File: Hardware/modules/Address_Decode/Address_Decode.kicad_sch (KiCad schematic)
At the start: 28 parts, among them J1 Bus_PCI_6502, J2 Clock_Sel, SW1 Manual_Clock, U1 74HC14, U2 74HC00, U3 74LS20, U4 DS1501YZ, U5 74LS393, U6 74HC138, U7 74HC688, X1 8MHz, Y1 G33270007

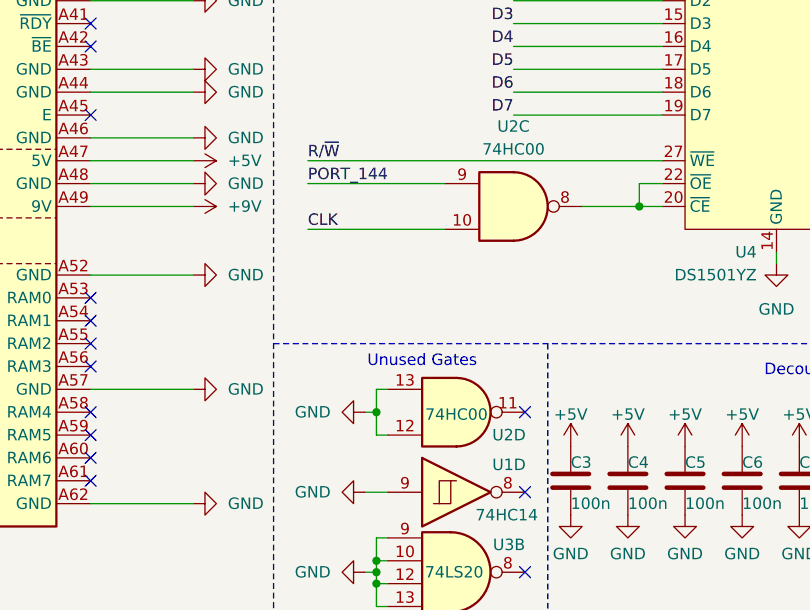
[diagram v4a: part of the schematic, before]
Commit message: update address decode
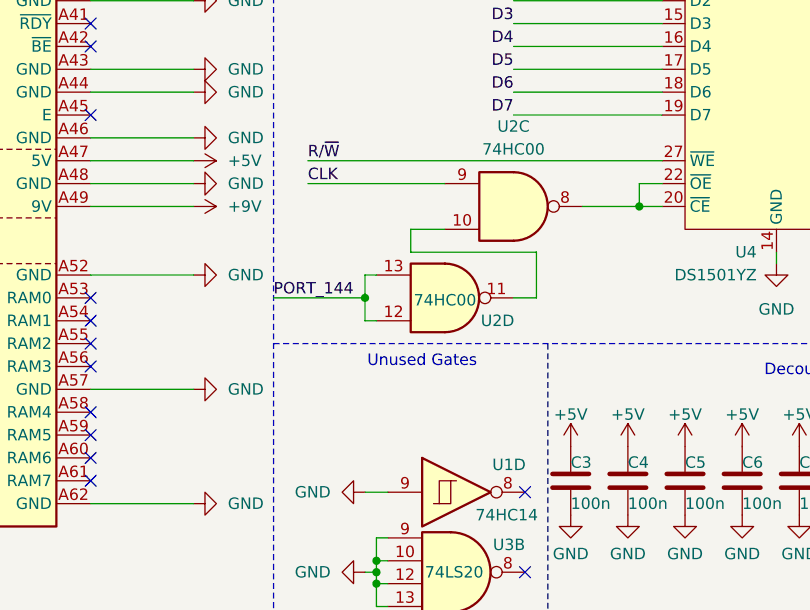
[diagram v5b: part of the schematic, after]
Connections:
- net CLK: now also U2.9; no longer U2.10
- net GND: no longer U2.12, U2.13
- net PORT_144: now also U2.12, U2.13; no longer U2.9
- net at U2.11: now also U2.10
- no-connect marks 50 -> 49
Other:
- moved on the sheet: U2D
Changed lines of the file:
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@@
 	)
 	(junction
-		(at 101.6 173.99)
+		(at 266.7 156.21)
 		(diameter 0)
 		(color 0 0 0 0)
 	)
 	(junction
-		(at 266.7 156.21)
+		(at 101.6 190.5)
 		(diameter 0)
 		(color 0 0 0 0)
 	)
 	(junction
-		(at 101.6 190.5)
+		(at 100.33 161.29)
 		(diameter 0)
 		(color 0 0 0 0)
@@
 	)
 	(no_connect
-		(at 118.11 173.99)
-	)
-	(no_connect
 		(at 120.65 73.66)
 	)
@@
 	(wire
 		(pts
-			(xy 101.6 173.99) (xy 101.6 176.53)
+			(xy 208.28 148.59) (xy 213.36 148.59)
 		)
 		(stroke
@@
 	(wire
 		(pts
-			(xy 208.28 148.59) (xy 213.36 148.59)
+			(xy 171.45 35.56) (xy 177.8 35.56)
 		)
 		(stroke
@@
 	(wire
 		(pts
-			(xy 171.45 35.56) (xy 177.8 35.56)
+			(xy 22.86 140.97) (xy 34.29 140.97)
 		)
 		(stroke
@@
 	(wire
 		(pts
-			(xy 22.86 140.97) (xy 34.29 140.97)
+			(xy 81.28 148.59) (xy 69.85 148.59)
 		)
 		(stroke
@@
 	(wire
 		(pts
-			(xy 81.28 148.59) (xy 69.85 148.59)
+			(xy 105.41 153.67) (xy 109.22 153.67)
+		)
+		(stroke
+			(width 0)
+			(type default)
+		)
+	)
+	(wire
+		(pts
+			(xy 105.41 156.21) (xy 105.41 153.67)
 		)
 		(stroke
@@
 	(wire
 		(pts
+			(xy 100.33 163.83) (xy 100.33 161.29)
+		)
+		(stroke
+			(width 0)
+			(type default)
+		)
+	)
+	(wire
+		(pts
 			(xy 215.9 49.53) (xy 215.9 45.72)
 		)
@@
 	(wire
 		(pts
+			(xy 100.33 158.75) (xy 101.6 158.75)
+		)
+		(stroke
+			(width 0)
+			(type default)
+		)
+	)
+	(wire
+		(pts
 			(xy 74.93 69.85) (xy 69.85 69.85)
 		)
@@
 	(wire
 		(pts
+			(xy 101.6 163.83) (xy 100.33 163.83)
+		)
+		(stroke
+			(width 0)
+			(type default)
+		)
+	)
+	(wire
+		(pts
 			(xy 231.14 72.39) (xy 238.76 72.39)
 		)
@@
 	(wire
 		(pts
-			(xy 101.6 176.53) (xy 102.87 176.53)
-		)
-		(stroke
-			(width 0)
-			(type default)
-		)
-	)
-	(wire
-		(pts
 			(xy 217.17 102.87) (xy 219.71 102.87)
 		)
@@
 	(wire
 		(pts
-			(xy 101.6 173.99) (xy 100.33 173.99)
-		)
-		(stroke
-			(width 0)
-			(type default)
-		)
-	)
-	(wire
-		(pts
 			(xy 74.93 54.61) (xy 69.85 54.61)
 		)
@@
 	(wire
 		(pts
+			(xy 100.33 161.29) (xy 100.33 158.75)
+		)
+		(stroke
+			(width 0)
+			(type default)
+		)
+	)
+	(wire
+		(pts
 			(xy 199.39 91.44) (xy 199.39 102.87)
 		)
@@
 	(wire
 		(pts
-			(xy 101.6 171.45) (xy 101.6 173.99)
-		)
-		(stroke
-			(width 0)
-			(type default)
-		)
-	)
-	(wire
-		(pts
 			(xy 274.32 105.41) (xy 271.78 105.41)
 		)
@@
 	(wire
 		(pts
+			(xy 116.84 161.29) (xy 119.38 161.29)
+		)
+		(stroke
+			(width 0)
+			(type default)
+		)
+	)
+	(wire
+		(pts
 			(xy 278.13 128.27) (xy 278.13 129.54)
 		)
@@
 	(wire
 		(pts
+			(xy 119.38 156.21) (xy 105.41 156.21)
+		)
+		(stroke
+			(width 0)
+			(type default)
+		)
+	)
+	(wire
+		(pts
 			(xy 176.53 48.26) (xy 176.53 50.8)
 		)
@@
 	(wire
 		(pts
-			(xy 109.22 148.59) (xy 93.98 148.59)
+			(xy 90.17 161.29) (xy 100.33 161.29)
 		)
 		(stroke
@@
 	(wire
 		(pts
-			(xy 93.98 153.67) (xy 109.22 153.67)
+			(xy 93.98 148.59) (xy 109.22 148.59)
 		)
 		(stroke
@@
 	(wire
 		(pts
-			(xy 101.6 171.45) (xy 102.87 171.45)
+			(xy 208.28 138.43) (xy 213.36 138.43)
 		)
 		(stroke
@@
 	(wire
 		(pts
-			(xy 208.28 138.43) (xy 213.36 138.43)
+			(xy 152.4 72.39) (xy 158.75 72.39)
 		)
 		(stroke
@@
 	(wire
 		(pts
-			(xy 152.4 72.39) (xy 158.75 72.39)
+			(xy 74.93 90.17) (xy 69.85 90.17)
 		)
 		(stroke
@@
 	(wire
 		(pts
-			(xy 74.93 90.17) (xy 69.85 90.17)
+			(xy 158.75 121.92) (xy 171.45 121.92)
 		)
 		(stroke
@@
 	(wire
 		(pts
-			(xy 158.75 121.92) (xy 171.45 121.92)
+			(xy 187.96 120.65) (xy 186.69 120.65)
 		)
 		(stroke
@@
 	(wire
 		(pts
-			(xy 187.96 120.65) (xy 186.69 120.65)
+			(xy 227.33 36.83) (xy 232.41 36.83)
 		)
 		(stroke
@@
 	(wire
 		(pts
-			(xy 227.33 36.83) (xy 232.41 36.83)
+			(xy 119.38 161.29) (xy 119.38 156.21)
 		)
 		(stroke
@@
 	)
 	(label "CLK"
-		(at 93.98 153.67 0)
+		(at 93.98 148.59 0)
 		(fields_autoplaced yes)
 		(effects
@@
 	)
 	(label "PORT_144"
-		(at 93.98 148.59 0)
+		(at 90.17 161.29 0)
 		(fields_autoplaced yes)
 		(effects
@@
 	(symbol
 		(lib_id "74xx:74HC00")
-		(at 110.49 173.99 0)
+		(at 109.22 161.29 0)
 		(mirror x)
 		(unit 4)
@@
 		(dnp no)
 		(property "Reference" "U2"
-			(at 116.332 176.53 0)
+			(at 115.062 163.83 0)
 			(effects
 				(font
@@
 		)
 		(property "Value" "74HC00"
-			(at 110.49 174.244 0)
+			(at 109.22 161.544 0)
 			(effects
 				(font
@@
 		)
 		(property "Footprint" "Package_DIP:DIP-14_W7.62mm_LongPads"
-			(at 110.49 173.99 0)
+			(at 109.22 161.29 0)
 			(effects
 				(font
@@
 		)
 		(property "Datasheet" "http://www.ti.com/lit/gpn/sn74hc00"
-			(at 110.49 173.99 0)
+			(at 109.22 161.29 0)
 			(effects
 				(font
@@
 		)
 		(property "Description" "quad 2-input NAND gate"
-			(at 110.49 173.99 0)
+			(at 109.22 161.29 0)
 			(effects
 				(font
@@
 					(unit 1)
 				)
-			)
-		)
-	)
-	(symbol
-		(lib_id "power:GND")
-		(at 100.33 173.99 270)
-		(mirror x)
-		(unit 1)
-		(exclude_from_sim no)
-		(in_bom yes)
-		(on_board yes)
-		(dnp no)
-		(fields_autoplaced yes)
-		(property "Reference" "#PWR014"
-			(at 93.98 173.99 0)
-			(effects
-				(font
-					(size 1.27 1.27)
-				)
-				(hide yes)
-			)
-		)
-		(property "Value" "GND"
-			(at 96.52 173.9899 90)
-			(effects
-				(font
-					(size 1.27 1.27)
-				)
-				(justify right)
-			)
-		)
-		(property "Footprint" ""
-			(at 100.33 173.99 0)
-			(effects
-				(font
-					(size 1.27 1.27)
-				)
-				(hide yes)
-			)
-		)
-		(property "Datasheet" ""
-			(at 100.33 173.99 0)
-			(effects
-				(font
-					(size 1.27 1.27)
-				)
-				(hide yes)
-			)
-		)
-		(property "Description" "Power symbol creates a global label with name \"GND\" , ground"
-			(at 100.33 173.99 0)
-			(effects
-				(font
-					(size 1.27 1.27)
-				)
-				(hide yes)
-			)
-		)
-		(pin "1"
-		)
-		(instances
-			(project "Address_Decode"
-				(path "/a8f3be35-d595-4d09-a3be-a54adbc9e0af"
-					(reference "#PWR014")
-					(unit 1)
-				)
